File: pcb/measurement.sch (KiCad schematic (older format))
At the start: 20 parts

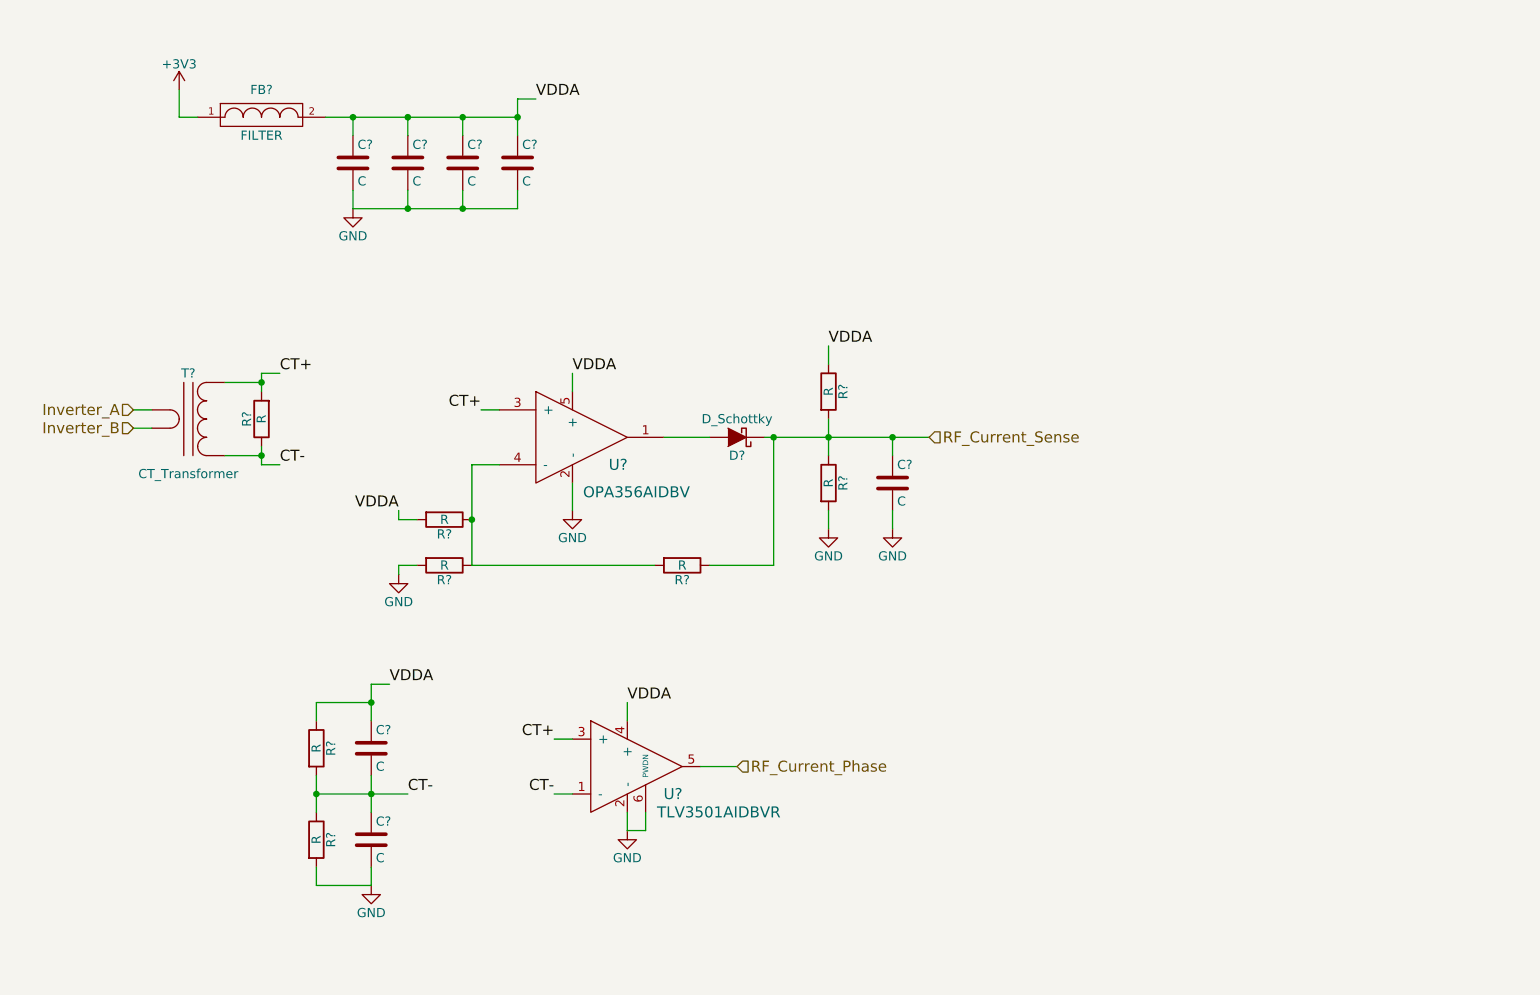
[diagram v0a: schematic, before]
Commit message: added measurements and simulation
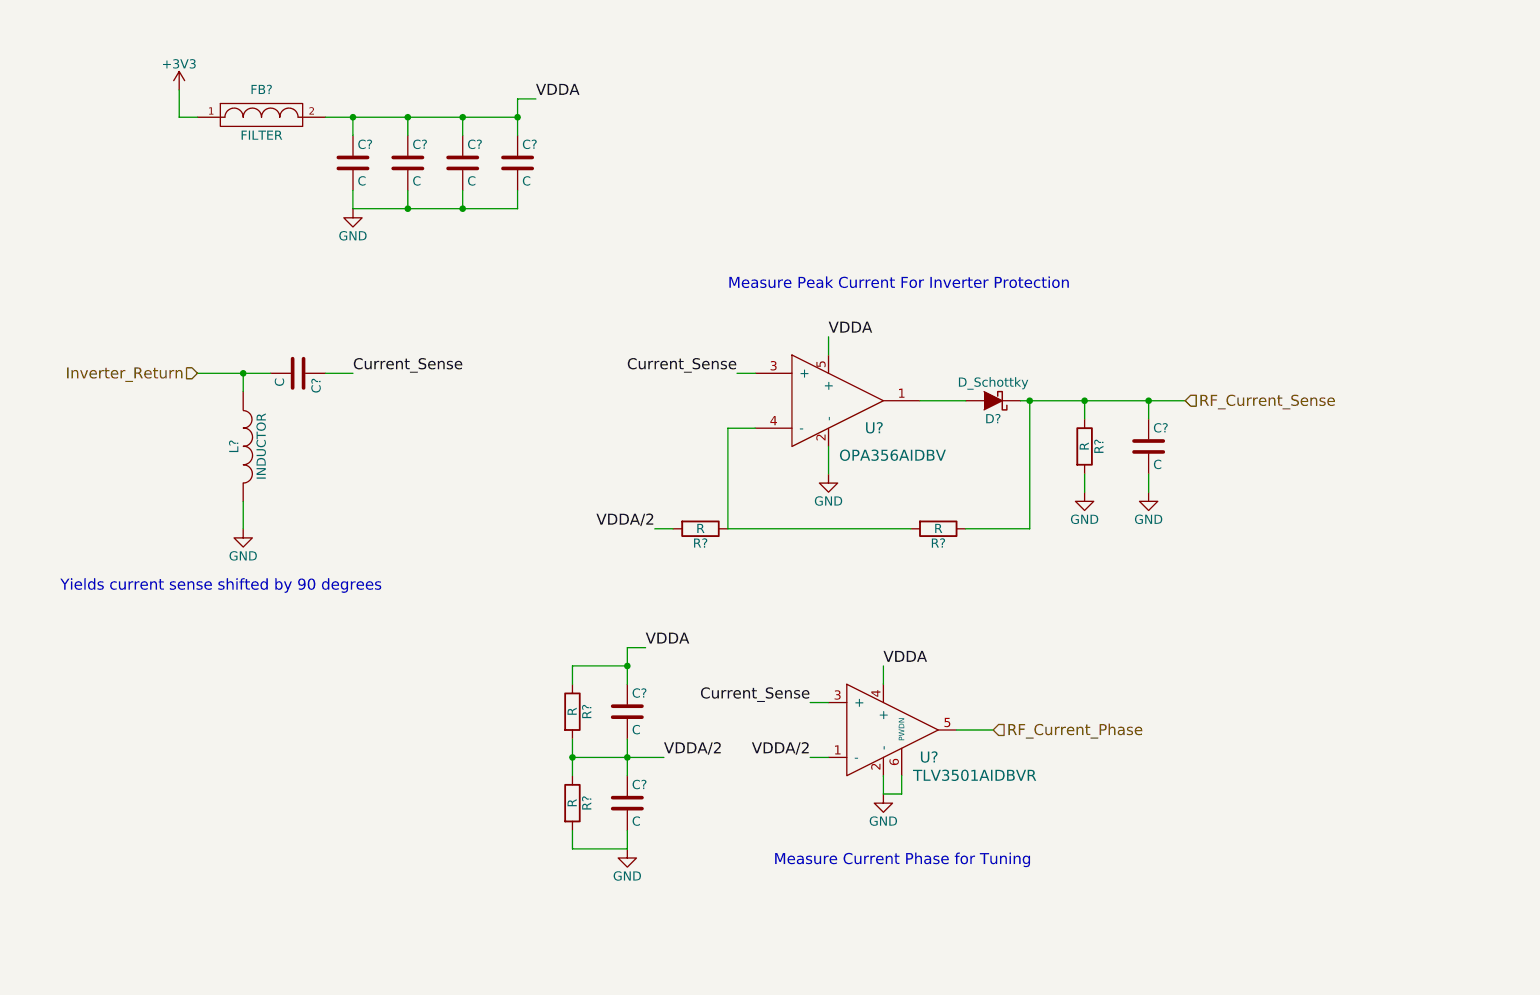
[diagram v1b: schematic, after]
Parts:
- removed R? (x3): R, symbol R
- removed T?: CT_Transformer, symbol CT_Transformer
- added C?: C, symbol C
- added L?: INDUCTOR, symbol INDUCTOR
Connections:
- net GND: now also L?.2; no longer R?.2
- net CT+ renamed Current_Sense
- net Current_Sense: now also C?.1
- net CT- renamed VDDA/2
- net VDDA/2: now also R?.2
- new net Inverter_Return: C?.2, L?.1
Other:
- note added: "Measure Current Phase for Tuning"
- note added: "Measure Peak Current For Inverter Protection"
- note added: "Yields current sense shifted by 90 degrees"
- moved on the sheet: C?, D?, R?, U?

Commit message: new GaN test board
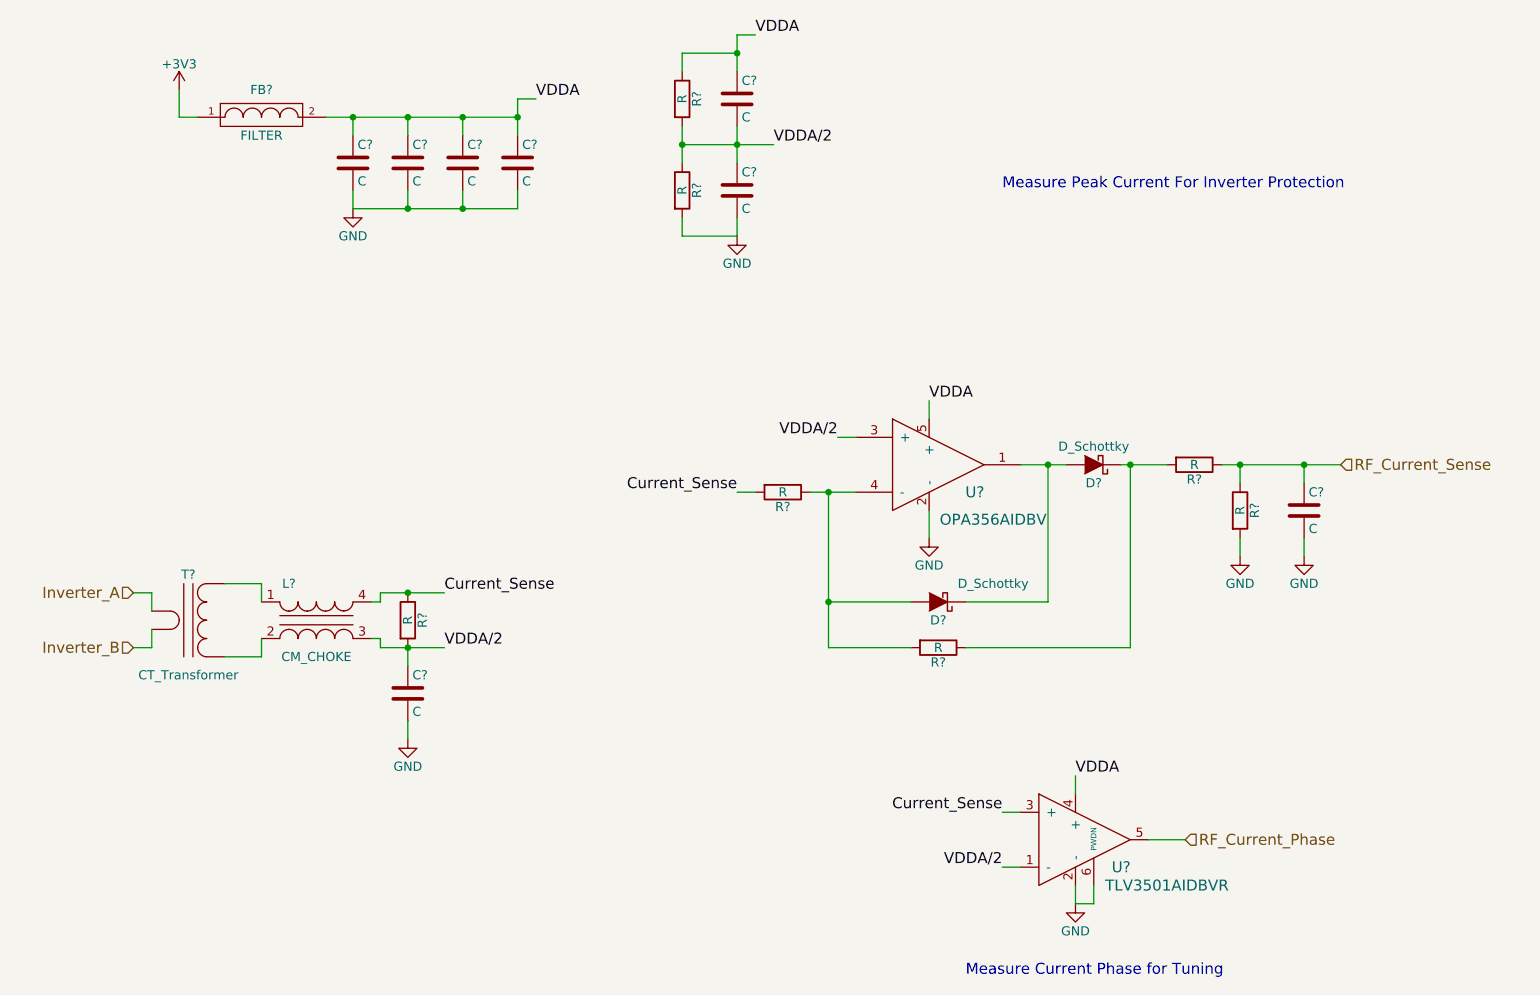
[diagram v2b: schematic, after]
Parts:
- removed C?: C, symbol C
- removed L?: INDUCTOR, symbol INDUCTOR
- removed R? (x2): R, symbol R
- added C?: C, symbol C
- added D?: D_Schottky, symbol D_Schottky
- added L?: CM_CHOKE, symbol CM_CHOKE
- added R? (x4): R, symbol R
- added T?: CT_Transformer, symbol CT_Transformer
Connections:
- net Current_Sense: now also L?.4, R?.1, R?.2; no longer U?.3 (+)
- net GND: now also C?.2
- net RF_Current_Sense: now also R?.1; no longer D?.1 (K)
- net VDDA/2: now also U?.3 (+), C?.1, L?.3, R?.2
- net at D?.2 (A), U?.1: now also D?.1 (K)
- net at U?.4 (-): now also D?.2 (A), R?.1, R?.2
- new net: D?.1 (K), R?.1, R?.2
- new net: L?.1, T?.3
- new net: L?.2, T?.4
- new net Inverter_A: T?.1
- new net Inverter_B: T?.2
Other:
- note removed: "Yields current sense shifted by 90 degrees"
- moved on the sheet: C?, D?, R?, U?
